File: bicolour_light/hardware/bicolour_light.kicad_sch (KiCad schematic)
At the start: 6 parts, among them J1 PIN_A, J2 PIN_B

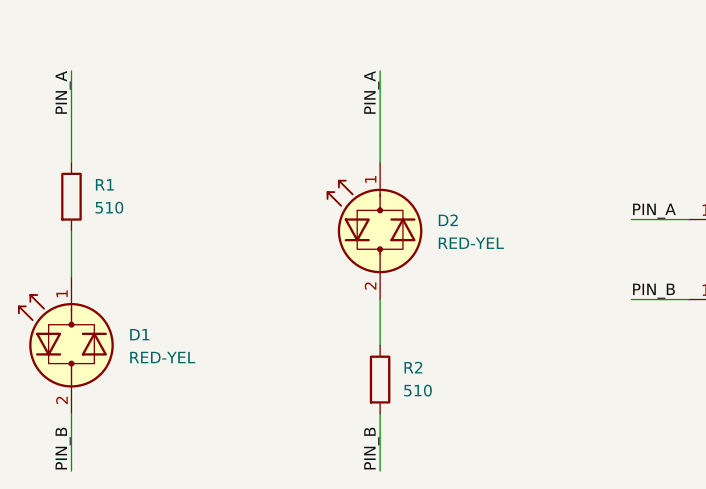
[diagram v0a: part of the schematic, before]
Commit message: Added polar light (single yellow LED)
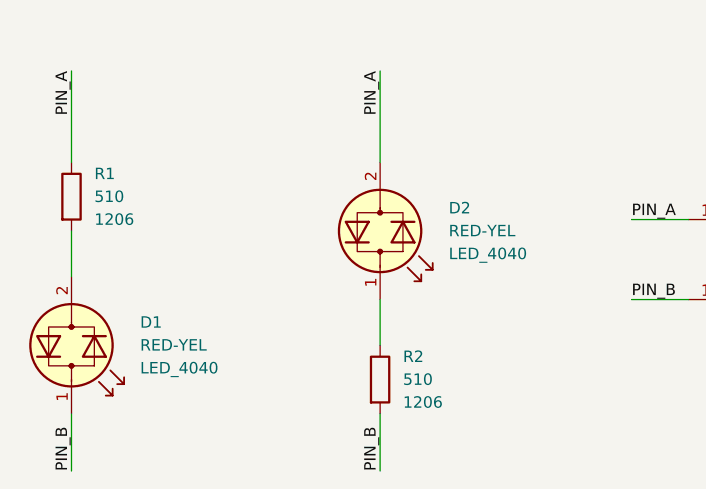
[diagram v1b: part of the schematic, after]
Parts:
- D1, D2: Package (none) -> LED_4040
- R1, R2: Package (none) -> 1206
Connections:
- net PIN_A: now also D2.2 (AK); no longer D2.1 (KA)
- net PIN_B: now also D1.1 (KA); no longer D1.2 (AK)
- net at R1.2: now also D1.2 (AK); no longer D1.1 (KA)
- net at R2.1: now also D2.1 (KA); no longer D2.2 (AK)
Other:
- moved on the sheet: D1, D2
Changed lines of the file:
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@@
   (symbol (lib_id "Device:R") (at 146.05 80.01 0) (unit 1)
     (in_bom yes) (on_board yes) (dnp no)
-    (property "Reference" "R1" (at 148.59 78.74 0)
+    (property "Reference" "R1" (at 148.59 77.47 0)
       (effects (font (size 1.27 1.27)) (justify left))
     )
-    (property "Value" "510" (at 148.59 81.28 0)
+    (property "Value" "510" (at 148.59 80.01 0)
       (effects (font (size 1.27 1.27)) (justify left))
     )
@@
       (effects (font (size 1.27 1.27)) hide)
     )
+    (property "Package" "1206" (at 148.59 82.55 0)
+      (effects (font (size 1.27 1.27)) (justify left))
+    )
     (pin "1")
     (pin "2")
@@
     )
   )
-  (symbol (lib_id "Device:LED_Dual_Bidirectional") (at 146.05 96.52 90) (unit 1)
-    (in_bom yes) (on_board yes) (dnp no) (fields_autoplaced)
-    (property "Reference" "D1" (at 152.4 95.3897 90)
-      (effects (font (size 1.27 1.27)) (justify right))
+  (symbol (lib_id "Device:LED_Dual_Bidirectional") (at 146.05 96.52 270) (unit 1)
+    (in_bom yes) (on_board yes) (dnp no)
+    (property "Reference" "D1" (at 153.67 93.98 90)
+      (effects (font (size 1.27 1.27)) (justify left))
     )
-    (property "Value" "RED-YEL" (at 152.4 97.9297 90)
-      (effects (font (size 1.27 1.27)) (justify right))
+    (property "Value" "RED-YEL" (at 153.67 96.52 90)
+      (effects (font (size 1.27 1.27)) (justify left))
     )
     (property "Footprint" "Slonket_Footprints:D_LED_4040" (at 146.05 96.52 0)
@@
     (property "LCSC" "C7545694" (at 146.05 96.52 0)
       (effects (font (size 1.27 1.27)) hide)
+    )
+    (property "Package" "LED_4040" (at 153.67 99.06 90)
+      (effects (font (size 1.27 1.27)) (justify left))
     )
     (pin "1")
@@
     )
   )
-  (symbol (lib_id "Device:LED_Dual_Bidirectional") (at 180.34 83.82 90) (unit 1)
-    (in_bom yes) (on_board yes) (dnp no) (fields_autoplaced)
-    (property "Reference" "D2" (at 186.69 82.6897 90)
-      (effects (font (size 1.27 1.27)) (justify right))
+  (symbol (lib_id "Device:LED_Dual_Bidirectional") (at 180.34 83.82 270) (unit 1)
+    (in_bom yes) (on_board yes) (dnp no)
+    (property "Reference" "D2" (at 187.96 81.28 90)
+      (effects (font (size 1.27 1.27)) (justify left))
     )
-    (property "Value" "RED-YEL" (at 186.69 85.2297 90)
-      (effects (font (size 1.27 1.27)) (justify right))
+    (property "Value" "RED-YEL" (at 187.96 83.82 90)
+      (effects (font (size 1.27 1.27)) (justify left))
     )
     (property "Footprint" "Slonket_Footprints:D_LED_4040" (at 180.34 83.82 0)
@@
     (property "LCSC" "C7545694" (at 180.34 83.82 0)
       (effects (font (size 1.27 1.27)) hide)
+    )
+    (property "Package" "LED_4040" (at 187.96 86.36 90)
+      (effects (font (size 1.27 1.27)) (justify left))
     )
     (pin "1")
@@
   (symbol (lib_id "Device:R") (at 180.34 100.33 0) (unit 1)
     (in_bom yes) (on_board yes) (dnp no)
-    (property "Reference" "R2" (at 182.88 99.06 0)
+    (property "Reference" "R2" (at 182.88 97.79 0)
       (effects (font (size 1.27 1.27)) (justify left))
     )
-    (property "Value" "510" (at 182.88 101.6 0)
+    (property "Value" "510" (at 182.88 100.33 0)
       (effects (font (size 1.27 1.27)) (justify left))
     )
@@
       (effects (font (size 1.27 1.27)) hide)
     )
+    (property "Package" "1206" (at 182.88 102.87 0)
+      (effects (font (size 1.27 1.27)) (justify left))
+    )
     (pin "1")
